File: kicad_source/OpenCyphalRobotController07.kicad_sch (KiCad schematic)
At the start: 23 parts, among them P1 SM04B-SRSS-TB, P2 RASPBERRYPI_PICO, P3 SM04B-SRSS-TB, P4 S3B-PH-SM4-TB, SW1 PTS636 SM43 SMTR LFS, U1 24LC64-I/SN

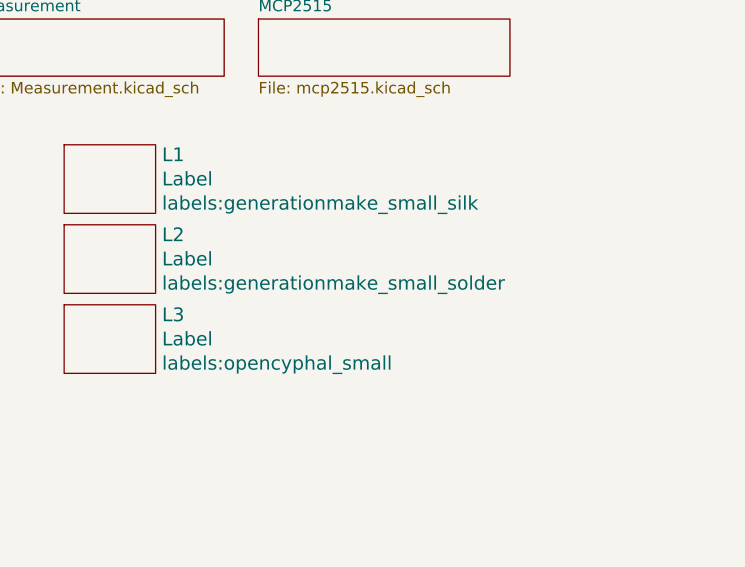
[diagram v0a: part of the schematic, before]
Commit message: updated layout
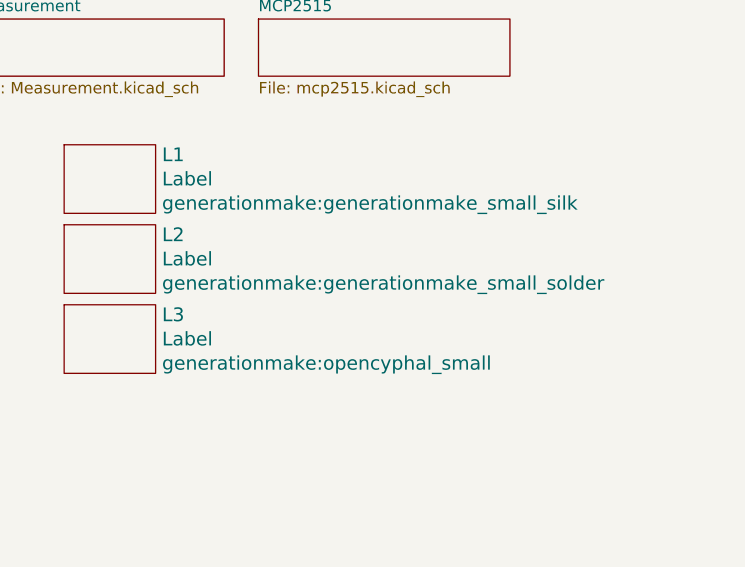
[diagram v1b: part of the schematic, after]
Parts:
- L1: footprint labels:generationmake_small_silk -> generationmake:generationmake_small_silk
- L2: footprint labels:generationmake_small_solder -> generationmake:generationmake_small_solder
- L3: footprint labels:opencyphal_small -> generationmake:opencyphal_small
- MECH1, MECH2, MECH3, MECH4: footprint MECH_mounting_holes:MHP_3.2_5.8 -> generationmake:MHP_3.2_5.8
- P2: footprint MODULE_compute:RASPI_PICO -> generationmake:RASPI_PICO_SOLDER_ONLY
- U1: footprint SOIC:SOIC-8_3.9x4.9mm_Pitch1.27mm -> Package_SO:SOIC-8_3.9x4.9mm_P1.27mm

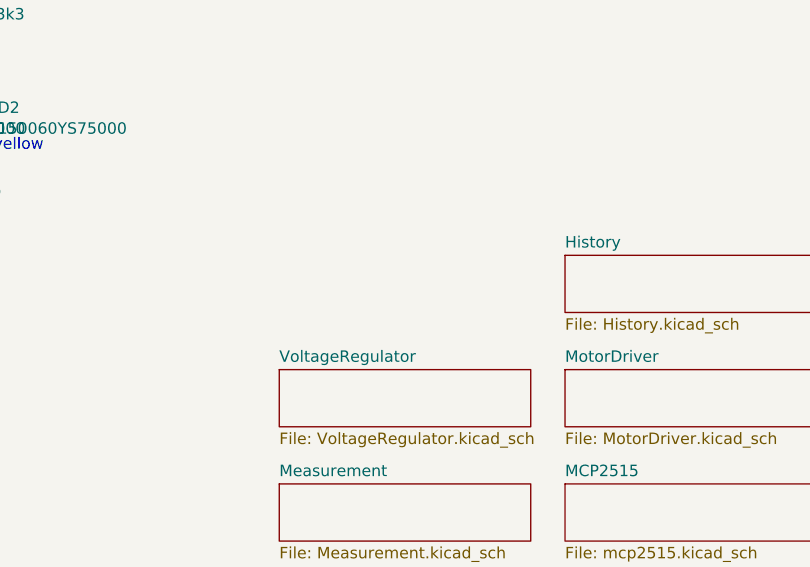
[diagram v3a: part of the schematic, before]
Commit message: added BNO085
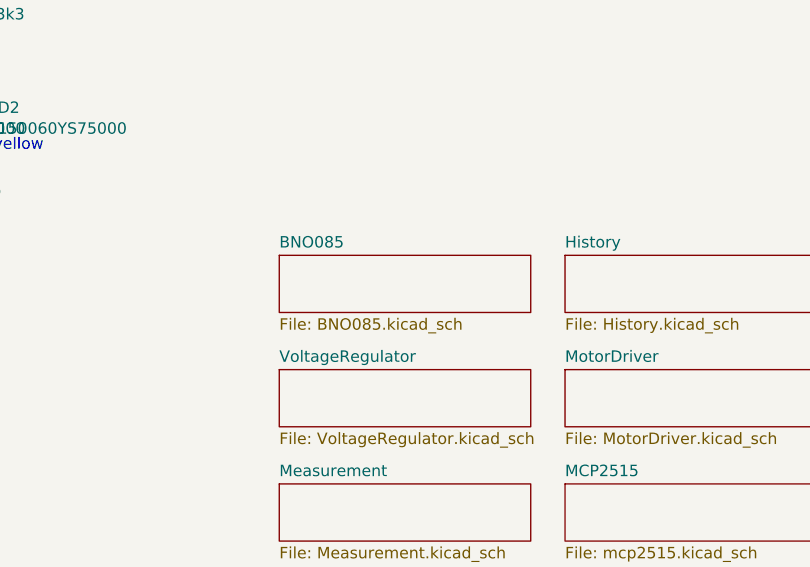
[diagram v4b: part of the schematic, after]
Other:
- added sheet BNO085 (BNO085.kicad_sch)

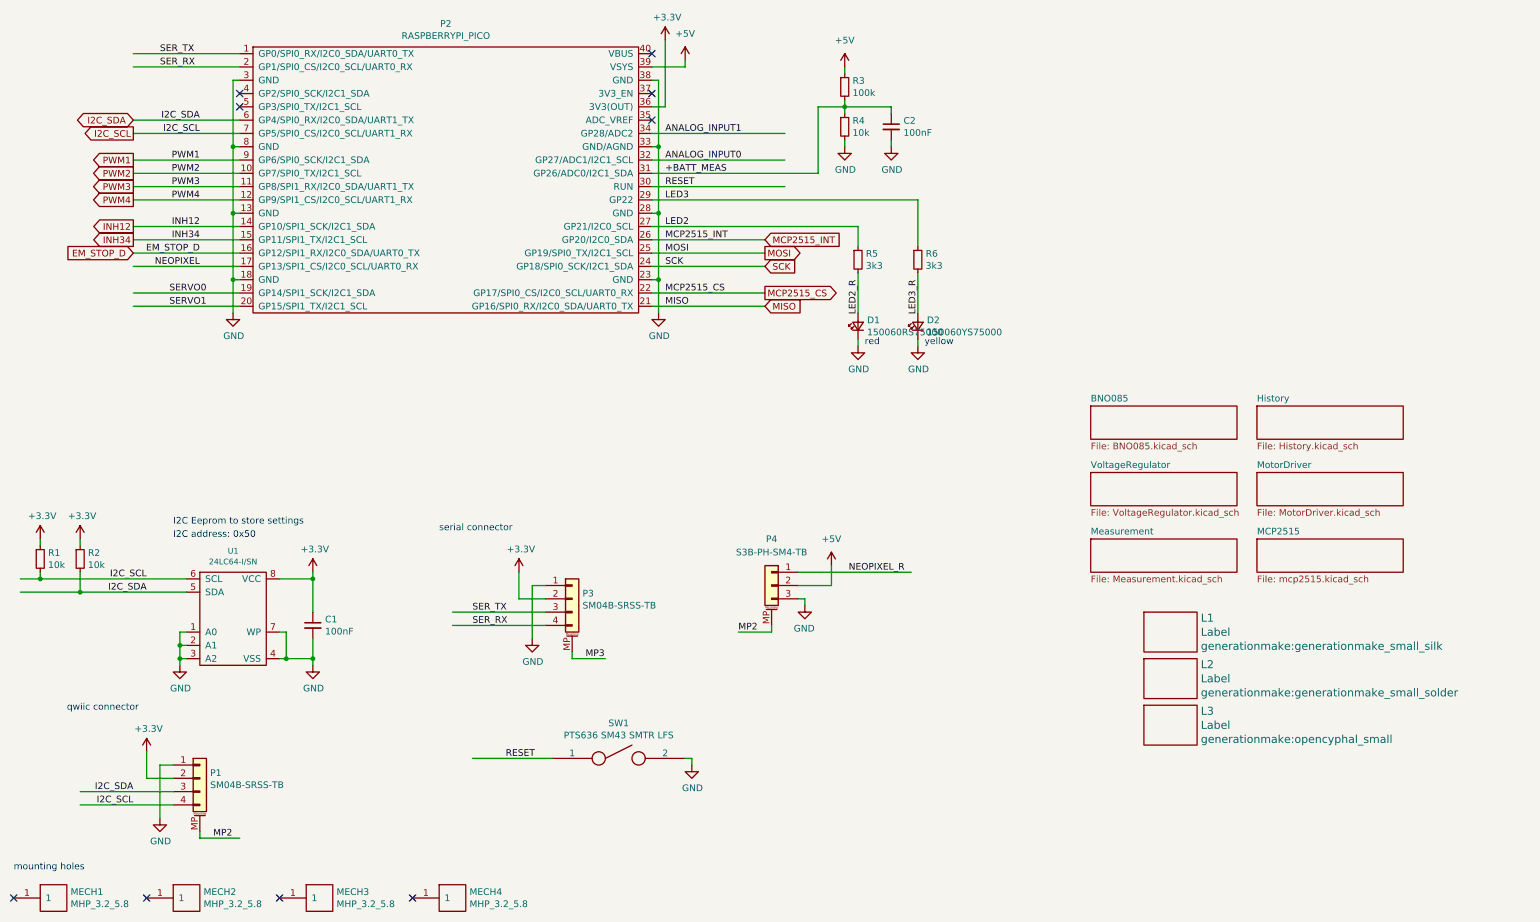
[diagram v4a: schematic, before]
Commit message: added page with outputs
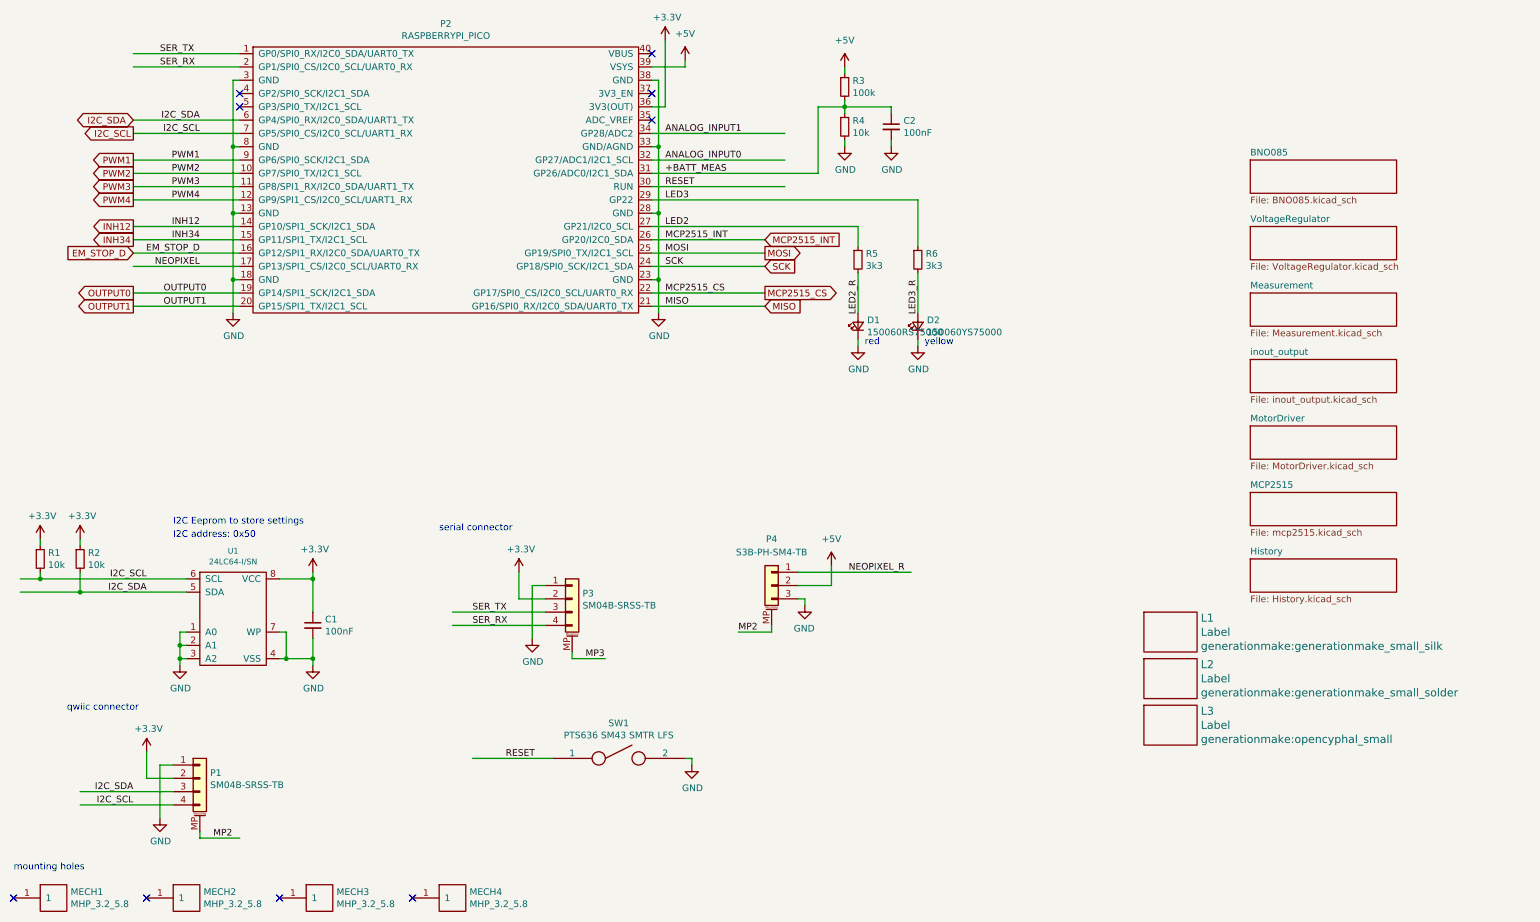
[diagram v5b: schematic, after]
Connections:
- net SERVO0 renamed OUTPUT0
- net SERVO1 renamed OUTPUT1
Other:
- added sheet inout_output (inout_output.kicad_sch)
- title: OpenCyphalRobotController07 -> CyphalRobotController07/CAN

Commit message: started layout
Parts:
- renumbered P1 to J1, P2 to J2, P3 to J3, P4 to J4
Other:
- moved on the sheet: L1, L2, L3
